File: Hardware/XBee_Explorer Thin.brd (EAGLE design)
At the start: 43.2 x 52.1 mm, 129 parts, among them J4 QWIIC_RIGHT_ANGLE, Q2 3.1A/30V/105mΩ, U1 FSUSB30MUX_MSOP10, U2 AP63203, U3 ESD Diode, U5 ESD Diode, U6 CP210X

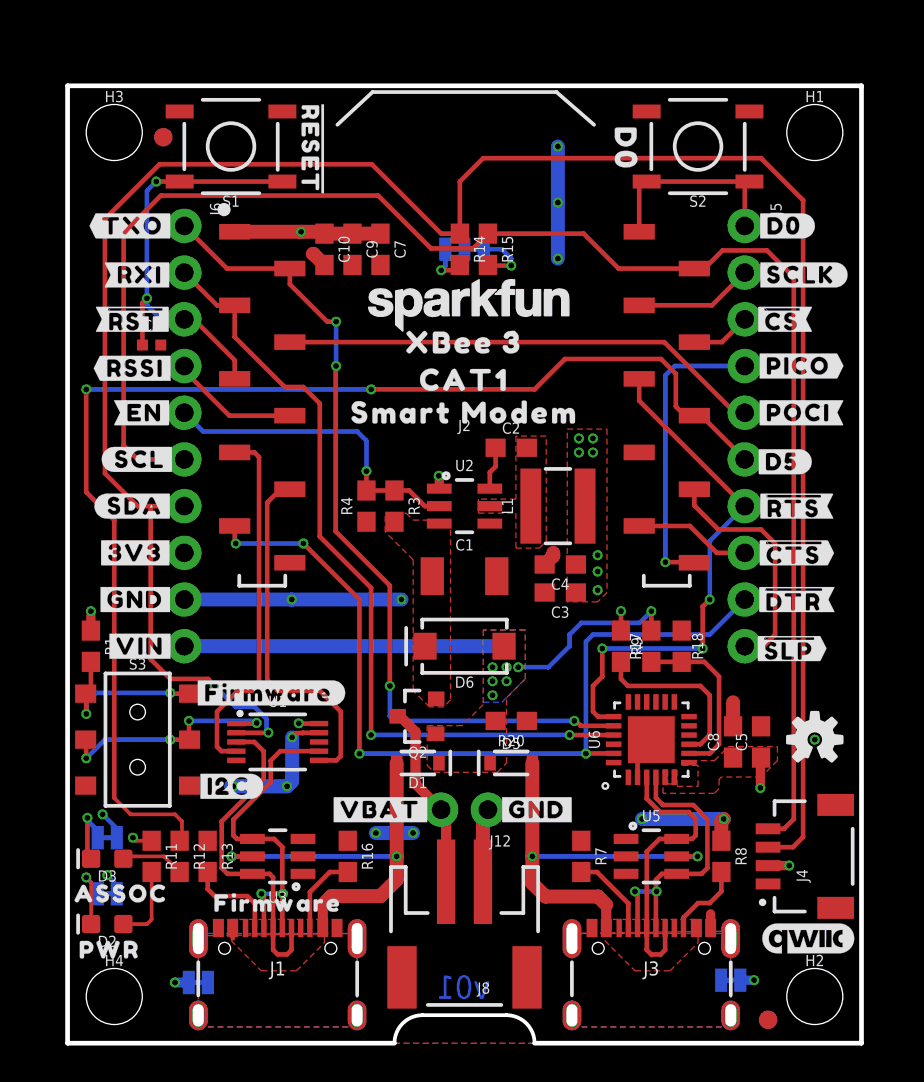
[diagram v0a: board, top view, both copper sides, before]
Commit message: Fixes various DRC issues
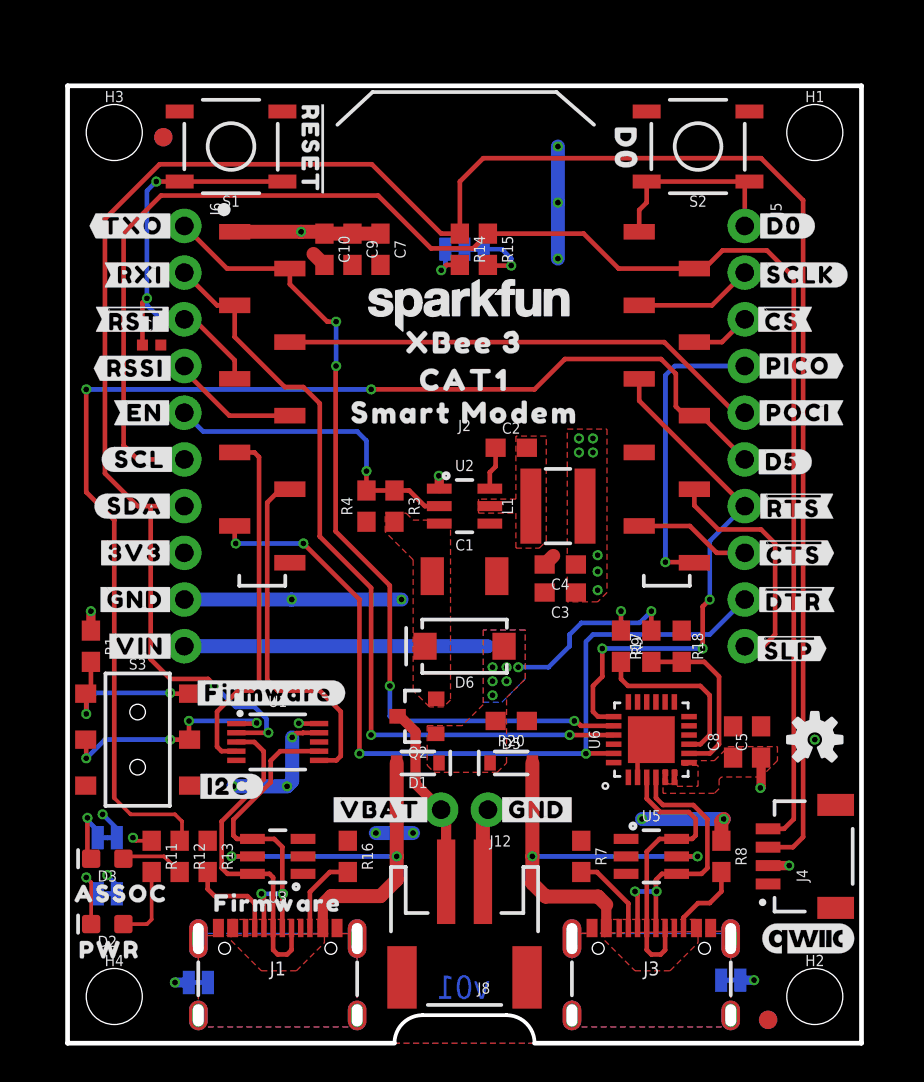
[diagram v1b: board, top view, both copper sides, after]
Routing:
- net GND: track 47.6 -> 45.1 mm
- net VIN: track 27.1 -> 26.4 mm
- net V_USB_2: track 22.9 -> 22.3 mm
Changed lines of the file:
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@@
 <drawing>
 <settings>
-<setting alwaysvectorfont="yes"/>
+<setting alwaysvectorfont="no"/>
 <setting verticaltext="up"/>
 </settings>
@@
 <wire x1="37.338" y1="3.429" x2="36.5887" y2="3.429" width="0.508" layer="16"/>
 <via x="37.338" y="3.429" extent="1-16" drill="0.3048"/>
-<wire x1="34.975" y1="6.264" x2="34.975" y2="7.035" width="0.508" layer="1"/>
 <wire x1="2.6797" y1="11.176" x2="2.6797" y2="11.6713" width="0.254" layer="16"/>
 <wire x1="2.6797" y1="11.6713" x2="1.905" y2="12.446" width="0.254" layer="16"/>
@@
 <via x="18.161" y="24.13" extent="1-16" drill="0.3048"/>
 <wire x1="13.68" y1="16.883" x2="12.81134375" y2="16.883" width="0.254" layer="1"/>
-<wire x1="8.89" y1="13.97" x2="11.938" y2="13.97" width="0.762" layer="16"/>
 <via x="11.938" y="13.97" extent="1-16" drill="0.3048"/>
 <via x="16.764" y="11.43" extent="1-16" drill="0.3048"/>
-<wire x1="12.215065625" y1="16.637" x2="12.215065625" y2="16.533065625" width="0.254" layer="16"/>
 <wire x1="16.764" y1="11.43" x2="18.796" y2="11.43" width="0.762" layer="16"/>
 <via x="18.796" y="11.43" extent="1-16" drill="0.3048"/>
@@
 <wire x1="35.687" y1="12.192" x2="31.242" y2="12.192" width="0.762" layer="16"/>
 <via x="31.242" y="12.192" extent="1-16" drill="0.3048"/>
-<wire x1="36.195" y1="17.233" x2="36.195" y2="18.542" width="0.762" layer="1"/>
 <contactref element="J6" pad="9"/>
 <wire x1="12.192" y1="24.13" x2="6.35" y2="24.13" width="0.762" layer="16"/>
@@
 <wire x1="12.443665625" y1="16.8656" x2="12.215065625" y2="16.637" width="0.254" layer="1"/>
 <wire x1="25.947" y1="26.035" x2="26.416" y2="26.504" width="0.762" layer="1"/>
-<wire x1="26.416" y1="26.504" x2="26.416" y2="26.67" width="0.762" layer="1"/>
 <wire x1="26.67" y1="48.768" x2="26.67" y2="45.72" width="0.762" layer="16"/>
 <wire x1="26.67" y1="45.72" x2="26.67" y2="42.672" width="0.762" layer="16"/>
@@
 <wire x1="6.5913" y1="3.302" x2="5.842" y2="3.302" width="0.5588" layer="16"/>
 <wire x1="13.97" y1="42.33" x2="13.374" y2="42.926" width="0.762" layer="1"/>
-<wire x1="13.374" y1="42.926" x2="13.335" y2="42.926" width="0.762" layer="1"/>
 <via x="9.017" y="13.97" extent="1-16" drill="0.3048"/>
 <wire x1="2.6797" y1="8.128" x2="2.6797" y2="8.6233" width="0.2032" layer="16"/>
@@
 <via x="2.159" y="9.144" extent="1-16" drill="0.3048"/>
 <via x="40.64" y="16.51" extent="1-16" drill="0.3048"/>
+<wire x1="9.017" y1="13.97" x2="11.938" y2="13.97" width="0.762" layer="16"/>
 </signal>
 <signal name="3.3V">
@@
 <wire x1="38.1" y1="9.66" x2="39.251" y2="9.66" width="0.508" layer="1"/>
 <wire x1="37.68" y1="15.494" x2="37.719" y2="15.533" width="0.508" layer="1"/>
-<wire x1="37.68" y1="15.494" x2="37.68" y2="13.882003125" width="0.508" layer="1"/>
 <wire x1="13.68" y1="17.383" x2="12.589" y2="17.383" width="0.254" layer="1"/>
 <wire x1="12.589" y1="17.383" x2="12.573" y2="17.399" width="0.254" layer="1"/>
@@
 <wire x1="3.722" y1="11.01" x2="3.556" y2="11.176" width="0.2032" layer="1"/>
 <via x="3.556" y="11.176" extent="1-16" drill="0.3048"/>
-<wire x1="37.68" y1="13.882003125" x2="37.68" y2="13.882" width="0" layer="19" extent="1-1"/>
+<wire x1="37.719" y1="15.533" x2="37.719" y2="13.921" width="0.508" layer="1"/>
+<wire x1="37.719" y1="13.921" x2="37.68" y2="13.882" width="0.508" layer="1"/>
 </signal>
 <signal name="V_USB">
@@
 <contactref element="I2C_PU" pad="3"/>
 <contactref element="R14" pad="2"/>
-<wire x1="21.336" y1="42.33" x2="21.17" y2="42.164" width="0.254" layer="1"/>
-<wire x1="21.336" y1="42.33" x2="21.043" y2="42.037" width="0.254" layer="1"/>
-<wire x1="21.043" y1="42.037" x2="20.32" y2="42.037" width="0.254" layer="1"/>
 <via x="20.32" y="42.037" extent="1-16" drill="0.3048"/>
 <wire x1="20.32" y1="42.037" x2="20.5486" y2="42.2656" width="0.254" layer="16"/>
 <wire x1="20.5486" y1="42.2656" x2="20.5486" y2="43.18" width="0.254" layer="16"/>
+<wire x1="21.336" y1="42.33" x2="20.613" y2="42.33" width="0.254" layer="1"/>
+<wire x1="20.613" y1="42.33" x2="20.32" y2="42.037" width="0.254" layer="1"/>
 </signal>
 <signal name="N$13">
@@
 <wire x1="32.385" y1="12.954" x2="32" y2="13.339" width="0.254" layer="1"/>
 <via x="32.0334" y="8.255" extent="1-16" drill="0.3048"/>
-<wire x1="31" y1="6.264" x2="30.988" y2="6.276" width="0.254" layer="1"/>
 <wire x1="31" y1="6.264" x2="31" y2="8.116" width="0.254" layer="1"/>
 <wire x1="31" y1="8.116" x2="30.861" y2="8.255" width="0.254" layer="1"/>
@@
 <wire x1="6.096" y1="46.863" x2="11.684" y2="46.863" width="0.254" layer="1"/>
 <wire x1="6.096" y1="46.863" x2="4.826" y2="46.863" width="0.254" layer="1"/>
-<wire x1="4.04045" y1="38.00455" x2="4.072" y2="37.973" width="0.254" layer="1"/>
 <via x="4.318" y="40.513" extent="1-16" drill="0.3048"/>
 <wire x1="4.318" y1="46.355" x2="4.318" y2="40.513" width="0.254" layer="16"/>
@@
 <wire x1="37.084" y1="46.863" x2="31.496" y2="46.863" width="0.254" layer="1"/>
 <contactref element="J2" pad="20"/>
-<wire x1="31.09" y1="44.13" x2="31.09" y2="46.761" width="0.254" layer="1"/>
-<wire x1="31.09" y1="46.761" x2="31.496" y2="46.863" width="0.254" layer="1"/>
+<wire x1="31.09" y1="44.13" x2="31.09" y2="45.314" width="0.254" layer="1"/>
+<wire x1="31.09" y1="45.314" x2="31.496" y2="45.72" width="0.254" layer="1"/>
+<wire x1="31.496" y1="45.72" x2="31.496" y2="46.863" width="0.254" layer="1"/>
 </signal>
 <signal name="N$7">
@@
 <wire x1="8.374" y1="15.883" x2="8.128" y2="16.129" width="0.254" layer="1"/>
 <wire x1="8.128" y1="16.129" x2="8.128" y2="18.034" width="0.254" layer="1"/>
-<wire x1="9.78" y1="32.13" x2="9.779" y2="32.131" width="0.254" layer="1"/>
 <wire x1="9.271" y1="19.177" x2="10.033" y2="19.177" width="0.254" layer="1"/>
 <wire x1="10.033" y1="19.177" x2="10.414" y2="19.558" width="0.254" layer="1"/>
@@
 <contactref element="D1" pad="A"/>
 <contactref element="U3" pad="5"/>
-<wire x1="8.98" y1="6.264" x2="8.98" y2="5.7007875" width="0.254" layer="1"/>
 <wire x1="13.88" y1="6.264" x2="13.88" y2="7.53" width="0.5588" layer="1"/>
 <wire x1="17.9" y1="8.883" x2="17.018" y2="8.001" width="0.762" layer="1"/>
@@
 <via x="31.75" y="23.495" extent="1-16" drill="0.3048"/>
 <contactref element="J6" pad="10"/>
-<wire x1="6.35" y1="21.59" x2="23.495" y2="21.59" width="0.762" layer="16"/>
 <via x="23.114" y="19.685" extent="1-16" drill="0.3048"/>
 <wire x1="31.75" y1="23.495" x2="31.115" y2="22.86" width="0.254" layer="16"/>
@@
 <via x="23.876" y="19.685" extent="1-16" drill="0.3048"/>
 <via x="23.114" y="18.923" extent="1-16" drill="0.3048"/>
+<wire x1="6.35" y1="21.59" x2="22.86" y2="21.59" width="0.762" layer="16"/>
 </signal>
 <signal name="N$21">
@@
 <contactref element="PLED" pad="2"/>
 <contactref element="D2" pad="C"/>
-<wire x1="1.282" y1="6.477" x2="1.282" y2="6.211" width="0.254" layer="1"/>
-<wire x1="1.651" y1="8.1153" x2="1.6383" y2="8.128" width="0.254" layer="16"/>
 <wire x1="1.282" y1="6.477" x2="1.282" y2="8.751" width="0.2032" layer="1"/>
 <wire x1="1.282" y1="8.751" x2="1.016" y2="9.017" width="0.2032" layer="1"/>
@@
 <wire x1="16.256" y1="30.06" x2="16.256" y2="31.115" width="0.254" layer="1"/>
 <via x="16.256" y="31.115" extent="1-16" drill="0.3048"/>
-<wire x1="16.256" y1="31.115" x2="16.256" y2="30.949" width="0.254" layer="16"/>
 <wire x1="17.78" y1="30.06" x2="18.581" y2="30.06" width="0.254" layer="1"/>
 <wire x1="17.78" y1="30.06" x2="16.256" y2="30.06" width="0.254" layer="1"/>

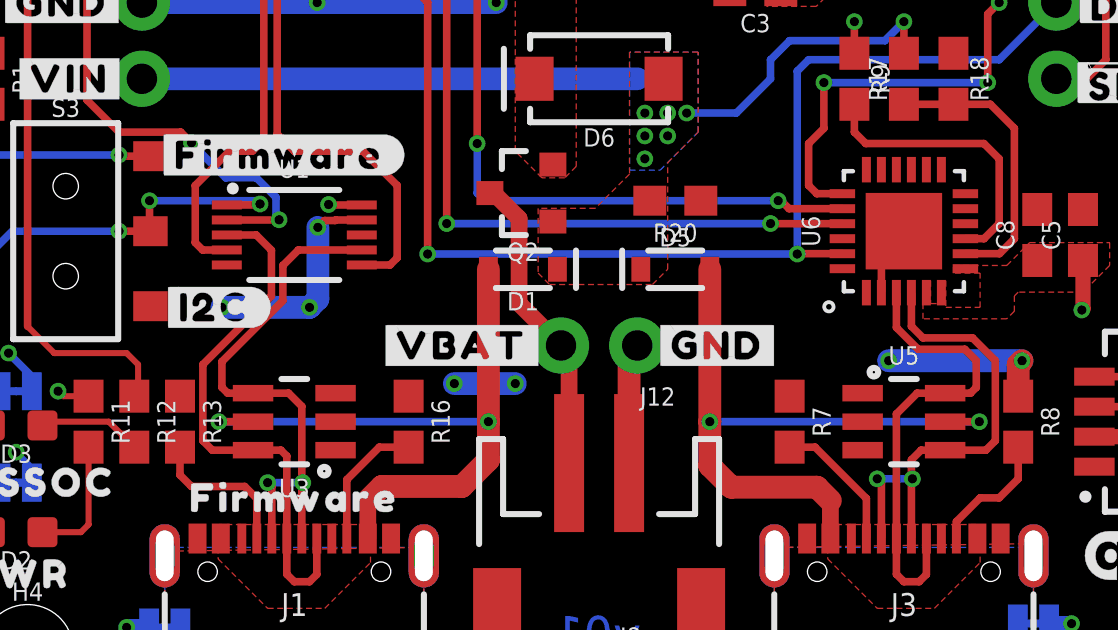
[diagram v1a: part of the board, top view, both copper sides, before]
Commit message: Fixes various schematic issues
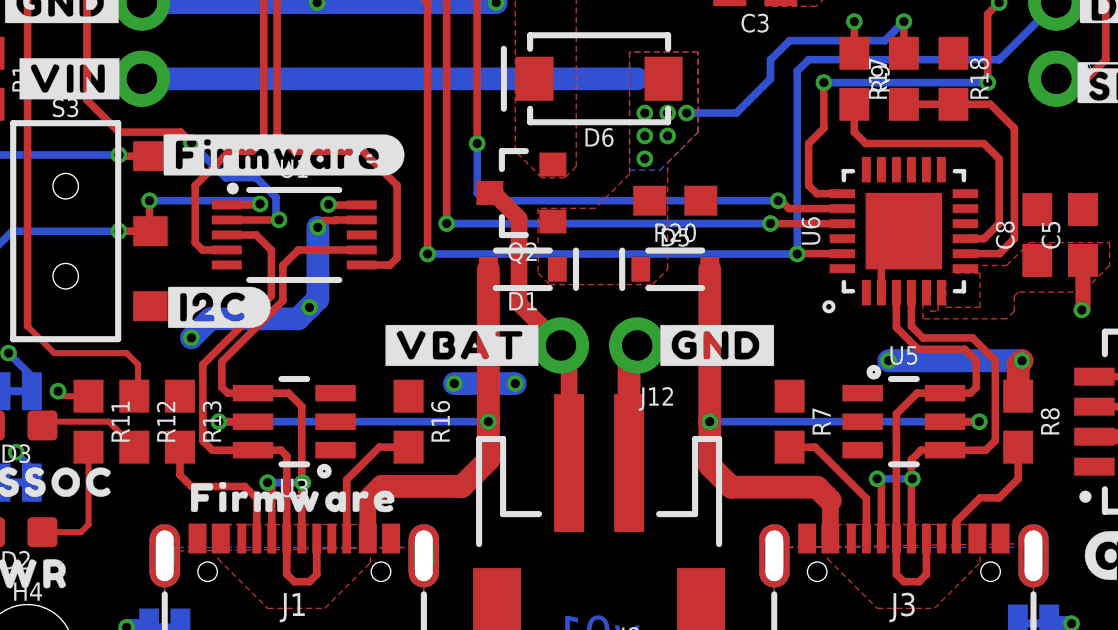
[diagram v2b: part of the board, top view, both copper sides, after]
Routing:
- net GND: track 45.1 -> 46.5 mm
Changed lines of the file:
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@@
 <wire x1="6.5913" y1="3.302" x2="5.842" y2="3.302" width="0.5588" layer="16"/>
 <wire x1="13.97" y1="42.33" x2="13.374" y2="42.926" width="0.762" layer="1"/>
-<via x="9.017" y="13.97" extent="1-16" drill="0.3048"/>
+<via x="8.001" y="12.954" extent="1-16" drill="0.3048"/>
 <wire x1="2.6797" y1="8.128" x2="2.6797" y2="8.6233" width="0.2032" layer="16"/>
 <wire x1="2.6797" y1="8.6233" x2="2.159" y2="9.144" width="0.2032" layer="16"/>
 <via x="2.159" y="9.144" extent="1-16" drill="0.3048"/>
 <via x="40.64" y="16.51" extent="1-16" drill="0.3048"/>
-<wire x1="9.017" y1="13.97" x2="11.938" y2="13.97" width="0.762" layer="16"/>
+<wire x1="11.557" y1="13.589" x2="11.938" y2="13.97" width="0.762" layer="16"/>
+<wire x1="11.557" y1="13.589" x2="8.636" y2="13.589" width="0.762" layer="16"/>
+<wire x1="8.001" y1="12.954" x2="8.636" y2="13.589" width="0.762" layer="16"/>
 </signal>
 <signal name="3.3V">
@@
 <vertex x="32.385" y="14.859"/>
 <vertex x="32.639" y="14.859"/>
-<vertex x="32.639" y="14.097"/>
-<vertex x="32.893" y="14.097"/>
+<vertex x="32.639" y="13.843"/>
+<vertex x="32.893" y="13.843"/>
 <vertex x="32.893" y="14.859"/>
 <vertex x="33.147" y="14.859"/>

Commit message: Adds two layers and many stitching vias
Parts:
- moved U$37 4.67 mm to (17.0, 12.7), turned to 0 degrees
- moved U$38 3.86 mm to (25.5, 12.7), turned to 0 degrees
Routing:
- net GND: track 46.5 -> 12.9 mm, vias 17 -> 51
- net 3.3V: track 15.9 -> 17.7 mm, vias 15 -> 16
- net VIN: vias 7 -> 5
- added copper zone on layer 15, net 3.3V
- added copper zone on layer 16, net GND
- added copper zone on layer 2, net GND
- removed copper zone on layer 16, net 3.3V

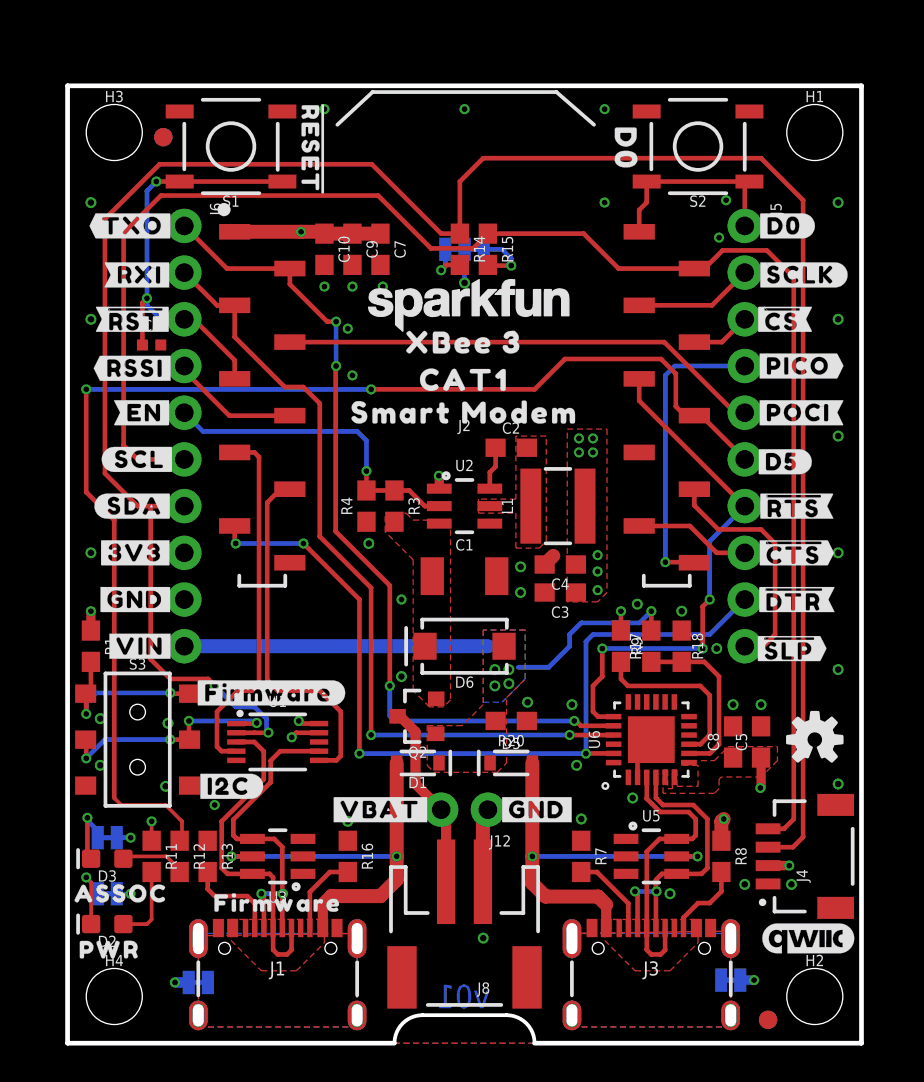
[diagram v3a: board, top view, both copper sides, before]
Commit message: Adds many vias, rearranges some part placement for better performance/routing
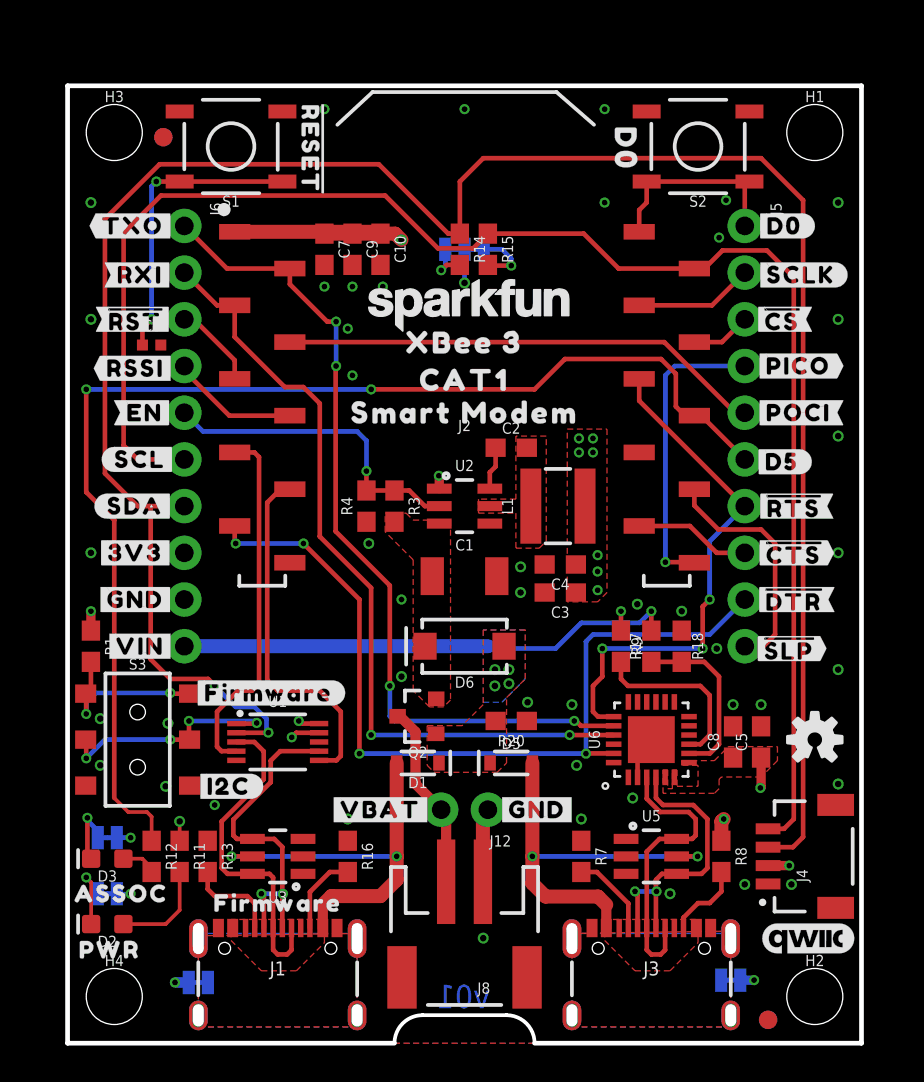
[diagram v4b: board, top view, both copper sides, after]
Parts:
- moved C10 3.05 mm to (17.0, 43.2)
- moved C7 3.05 mm to (14.0, 43.2)
- moved R11 1.52 mm to (6.10, 10.2)
- moved R12 1.52 mm to (4.57, 10.2)
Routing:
- net 3.3V: track 17.7 -> 22.0 mm
- net N$12: track 3.54 -> 1.96 mm
- net D5/ASSOCIATE: track 68.0 -> 66.4 mm
- net N$7: track 4.22 -> 5.45 mm
- net !RESET!: track 23.5 -> 22.5 mm
- net VIN: track 26.4 -> 25.8 mm
- net GND: track 12.9 -> 12.2 mm
